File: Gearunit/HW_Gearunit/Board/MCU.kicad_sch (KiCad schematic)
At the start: 4 parts, among them J5 Conn_01x05, U1 STM32L432KBUx

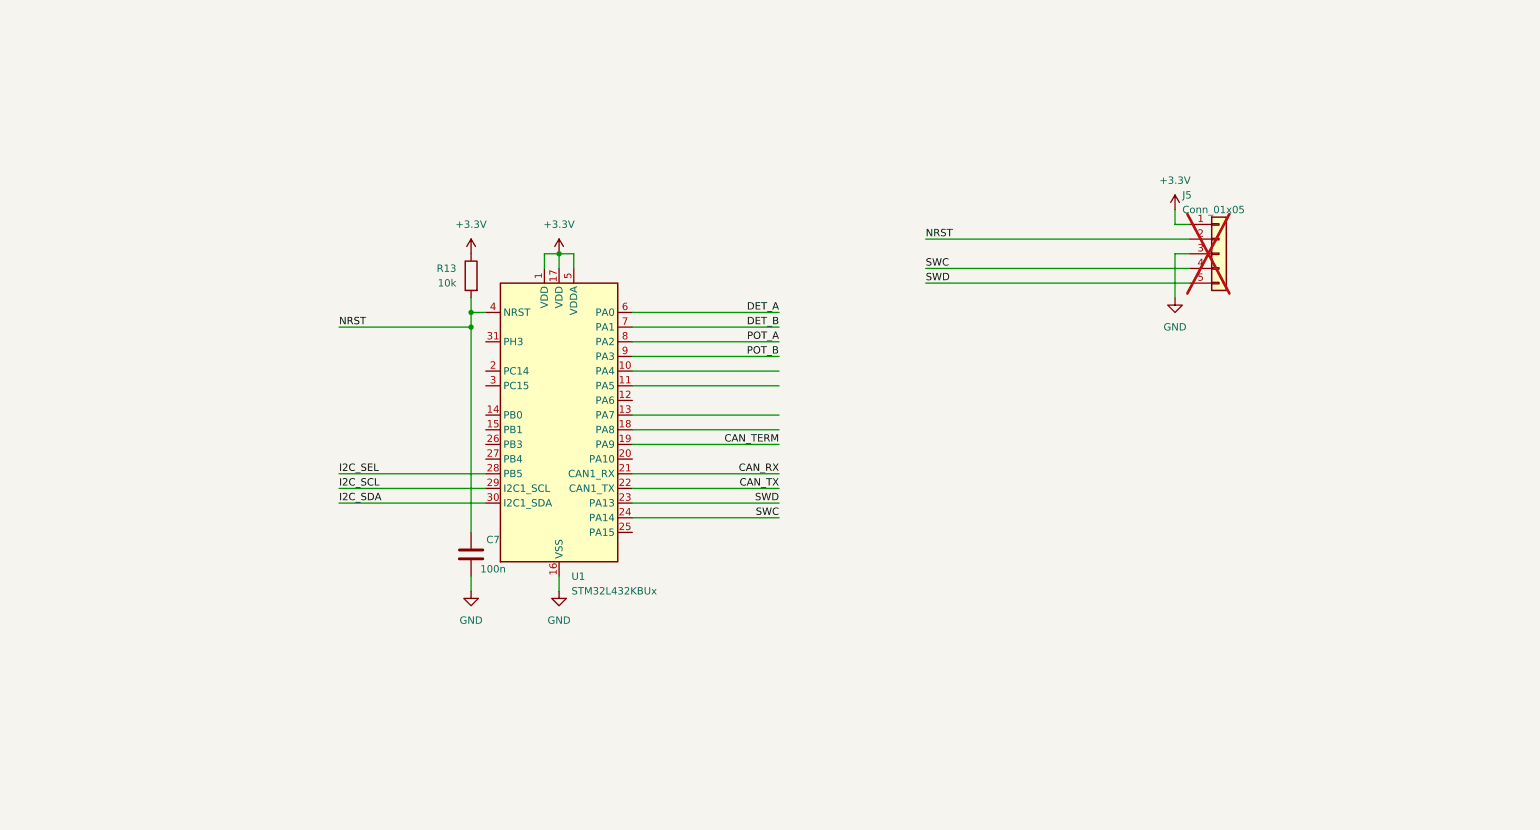
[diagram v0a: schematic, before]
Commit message: Gearunit updates, Readme updated
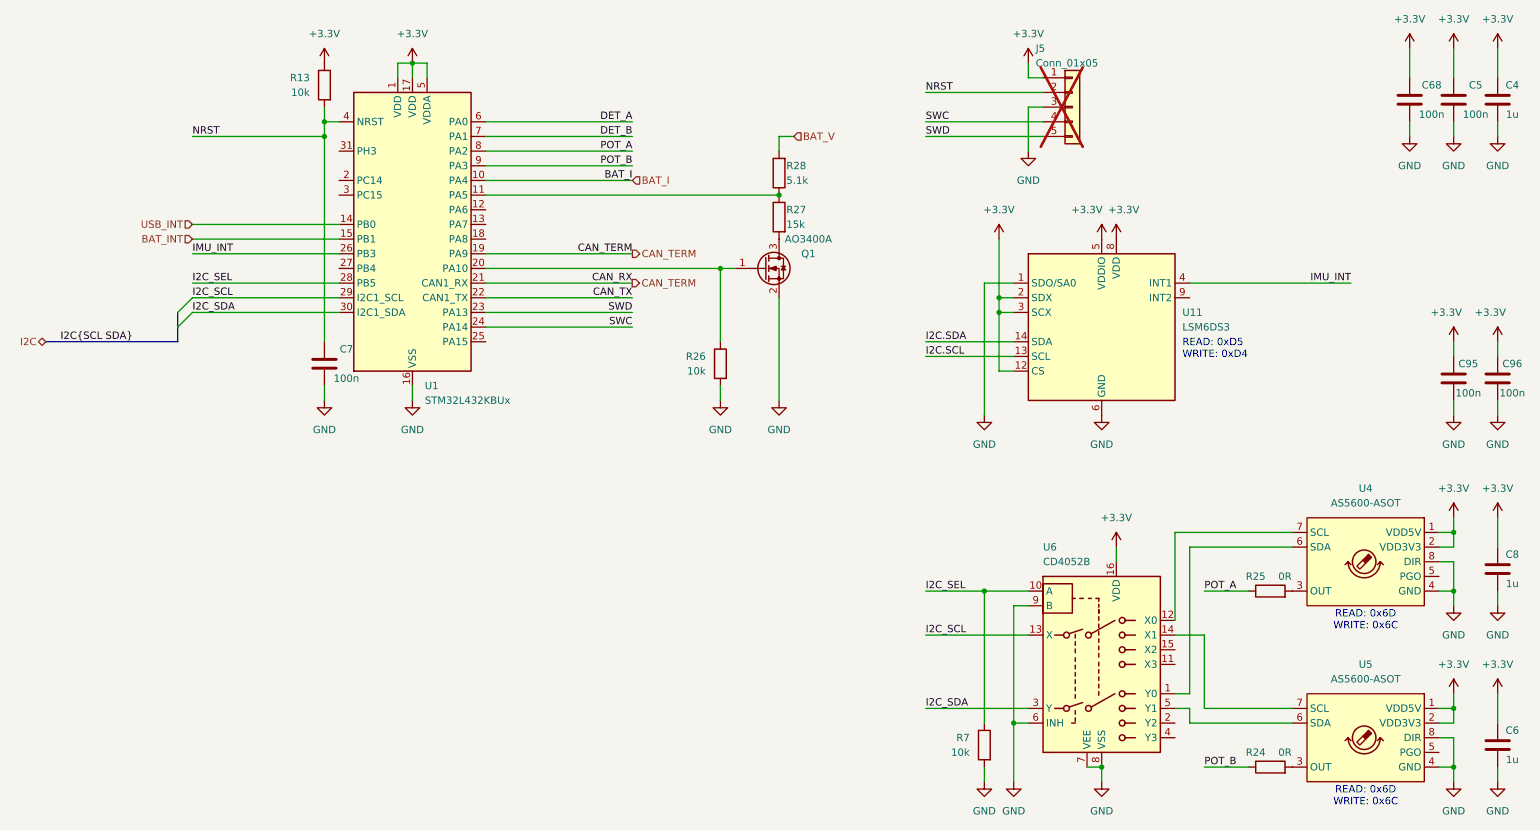
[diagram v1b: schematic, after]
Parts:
- added C4, C6, C8: 1u, Capacitor_SMD:C_0603_1608Metric, symbol Device:C
- added C5, C68, C95, C96: 100n, Capacitor_SMD:C_0402_1005Metric, symbol Device:C
- added Q1: AO3400A, Package_TO_SOT_SMD:SOT-23, symbol Transistor_FET:AO3400A
- added R24, R25: 0R, Resistor_SMD:R_0402_1005Metric, symbol Device:R
- added R26, R7: 10k, Resistor_SMD:R_0402_1005Metric, symbol Device:R
- added R27: 15k, Resistor_SMD:R_0402_1005Metric, symbol Device:R
- added R28: 5.1k, Resistor_SMD:R_0402_1005Metric, symbol Device:R
- added U11: LSM6DS3, Package_LGA:LGA-14_3x2.5mm_P0.5mm_LayoutBorder3x4y, symbol Sensor_Motion:LSM6DS3
- added U4, U5: AS5600-ASOT, Package_SO:SO-8_3.9x4.9mm_P1.27mm, symbol USER:AS5600-ASOT
- added U6: CD4052B, Package_SO:TSSOP-16_4.4x5mm_P0.65mm, symbol Analog_Switch:CD4052B
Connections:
- net CAN_RX is gone; now on net CAN_TERM: U1.21 (PA11)
- net +3.3V: now also C4.2, C5.2, C6.2, C68.2, C8.2, C95.1, C96.1, U11.12 (CS), U11.2 (SDX), U11.3 (SCX), U11.5 (VDDIO), U11.8 (VDD), U4.1 (VDD5V), U4.2 (VDD3V3), U5.1 (VDD5V), U5.2 (VDD3V3), U6.16 (VDD)
- net GND: now also C4.1, C5.1, C6.1, C68.1, C8.1, C95.2, C96.2, Q1.2 (S), R26.2, R7.2, U11.1 (SDO/SA0), U11.6 (GND), U11.7 (GND), U4.4 (GND), U4.8 (DIR), U5.4 (GND), U5.8 (DIR), U6.6 (INH), U6.7 (VEE), U6.8 (VSS), U6.9 (B)
- net I2C_SCL: now also U6.13 (X)
- net I2C_SDA: now also U6.3 (Y)
- net I2C_SEL: now also R7.1, U6.10 (A)
- net POT_A: now also R25.1
- net POT_B: now also R24.1
- net BAT_I: now reaches U1.10 (PA4)
- net at U1.11 (PA5): now also R27.1, R28.1
- net USB_INT: now reaches U1.14 (PB0)
- net BAT_INT: now reaches U1.15 (PB1)
- net at U1.20 (PA10): now also Q1.1 (G), R26.1
- net IMU_INT: now reaches U1.26 (PB3)
- net IMU_INT: now also U11.4 (INT1)
- new net: R24.2, U5.3 (OUT)
- new net: U5.6 (SDA), U6.5 (Y1)
- new net: U5.7 (SCL), U6.14 (X1)
- new net: R25.2, U4.3 (OUT)
- new net: Q1.3 (D), R27.2
- new net: U4.6 (SDA), U6.1 (Y0)
- new net: U4.7 (SCL), U6.12 (X0)
- new net BAT_V: R28.2
- new net I2C.SCL: U11.13 (SCL)
- new net I2C.SDA: U11.14 (SDA)
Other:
- note added: "READ: 0x6D WRITE: 0x6C"
- note added: "READ: 0xD5 WRITE: 0xD4"
- moved on the sheet: C7, J5, R13, U1
